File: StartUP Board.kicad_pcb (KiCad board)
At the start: 2 copper layers, 47 x 63.5 mm, 24 parts, among them J1 KEYSW_CONN, U3 ANT13SECQE, U4 D1

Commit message: pcb board progress, schematic should be finalized
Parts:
- removed U4: D1, Package_SON:WSON-6-1EP_2x2mm_P0.65mm_EP1x1.6mm
- added U2: D1, Package_SON:WSON-6-1EP_2x2mm_P0.65mm_EP1x1.6mm, F.Cu at (47.8, 48.5)
- AUX_12V1: value PWR_12V -> 12V_Conn
- C1: value 0.1u -> C1
- C2, C3: value 0.1u -> C3
- C4: value 0.1u -> C4
- GPIO6: value FNR_CONN -> FNR_OUT
- J1: value KEYSW_CONN -> KEYSW_OUT
- R1: value 100k -> R1
- R10: value 30k -> R10
- R2: value 100k -> R2
- R3: value 100k -> R3
- R4: value 100k -> R4
- R5: value 10k -> R5
- R6: value 10k -> R6
- R7: value 10k -> R7
- R8: value 30k -> R8
- R9: value 30k -> R9
- moved R4 1.54 mm to (45.0, 50.0)
- moved C4 1.50 mm to (45.0, 46.8)
- moved REF** 1.41 mm to (38.0, 70.5)
- moved REF** 1.12 mm to (80.0, 70.5)
- moved R3 1.04 mm to (42.5, 50.0)
- moved C3 1.03 mm to (42.5, 46.8)
- moved R5 1.00 mm to (47.5, 54.0)
- moved R8 1.00 mm to (45.0, 54.0)
- moved R2 0.56 mm to (40.0, 50.0)
- moved R6 0.50 mm to (47.5, 57.0)
- moved R9 0.50 mm to (45.0, 57.0)
- moved REF** 0.50 mm to (80.0, 11.5)
- moved REF** 0.50 mm to (38.0, 11.5)
- moved C2 0.48 mm to (40.0, 46.8)
- moved R1 0.25 mm to (37.5, 50.0)
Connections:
- J1 pad 2: Net-(J1-Pin_2) -> Net-(J1-Pin_1)
- J1 pad 3: Net-(J1-Pin_3) -> Net-(J1-Pin_1)
- R10 pad 2: Net-(J1-Pin_3) -> Net-(J1-Pin_1)
- R6 pad 1: Net-(J1-Pin_2) -> Net-(J1-Pin_1)
- R7 pad 1: Net-(J1-Pin_3) -> Net-(J1-Pin_1)
- R9 pad 2: Net-(J1-Pin_2) -> Net-(J1-Pin_1)
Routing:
- net Net-(J1-Pin_1): track 1.50 -> 87.4 mm, vias 0 -> 4
- net /FNR_FWD: track 0.00 -> 38.5 mm, vias 0 -> 2
- net GND: track 0.00 -> 21.3 mm, vias 0 -> 10
- net /KEYSW_CHARGE: track 8.84 -> 26.4 mm
- net +12V: track 4.40 -> 21.5 mm
- net /KEYSW_MAIN: track 11.4 -> 25.0 mm
- net /KEYSW_AUX: track 15.3 -> 26.0 mm
- net /KEYSW_OFF: track 22.2 -> 26.3 mm
- net /FNR_REV: track 36.9 -> 33.6 mm, vias 0 -> 2
- net Net-(J1-Pin_2): track 1.54 -> 0.00 mm
- net Net-(J1-Pin_3): track 1.50 -> 0.00 mm
- added copper zone on B.Cu, net GND
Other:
- board size 47 x 63.5 mm -> 47 x 64 mm
- board text added: "C2"
- board text added: "R1"
- board text added: "empty space below, is bad?"
- board text added: "questions: trace widths correct? used .5mm for 12V and then .3 for everything else holes bad? add CE and DE connectors for e-stop button? via locations weird? this is e stop hole"
- board text added: "to do: add psr stuff"

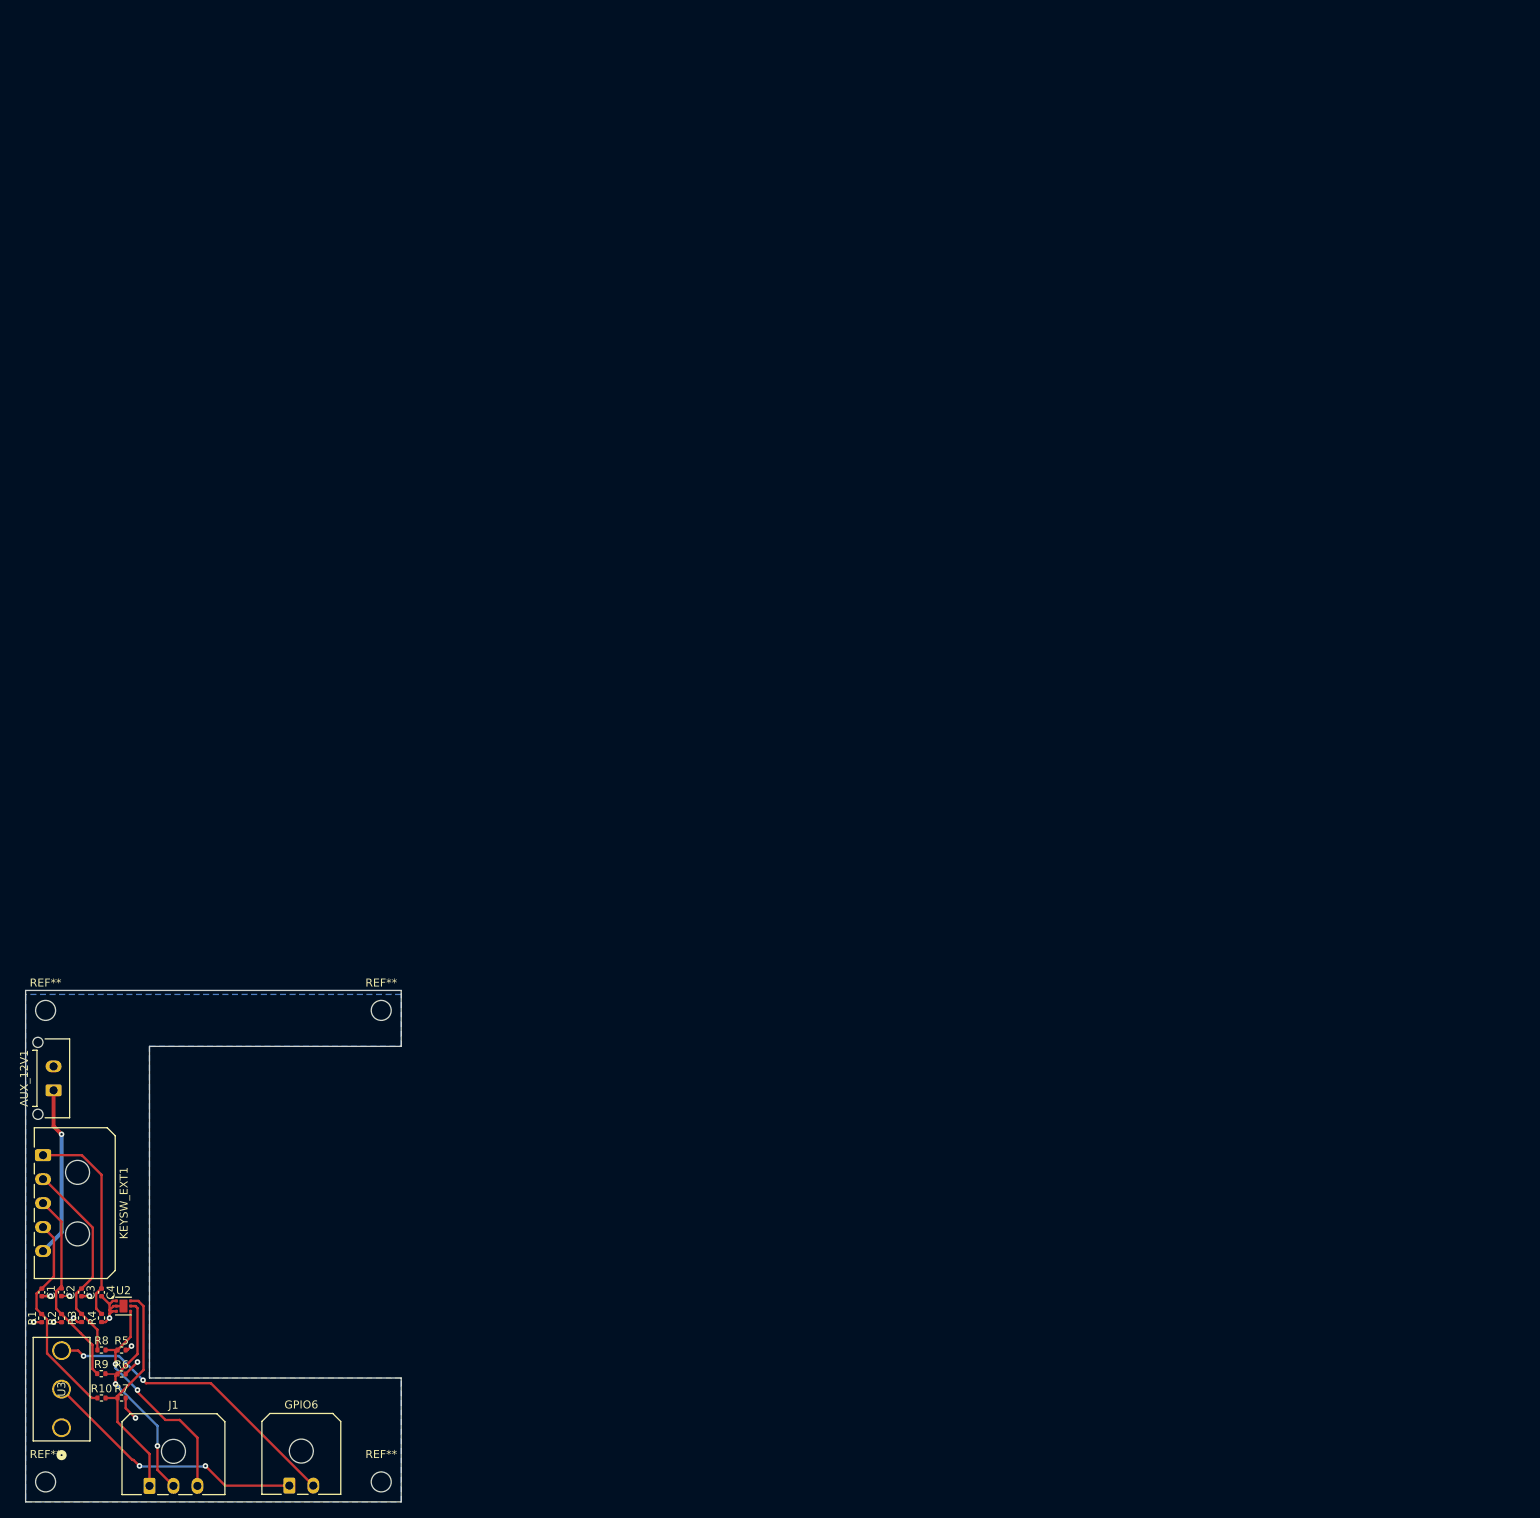
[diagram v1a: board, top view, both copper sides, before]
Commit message: Updated PCB layout, added mounting holes
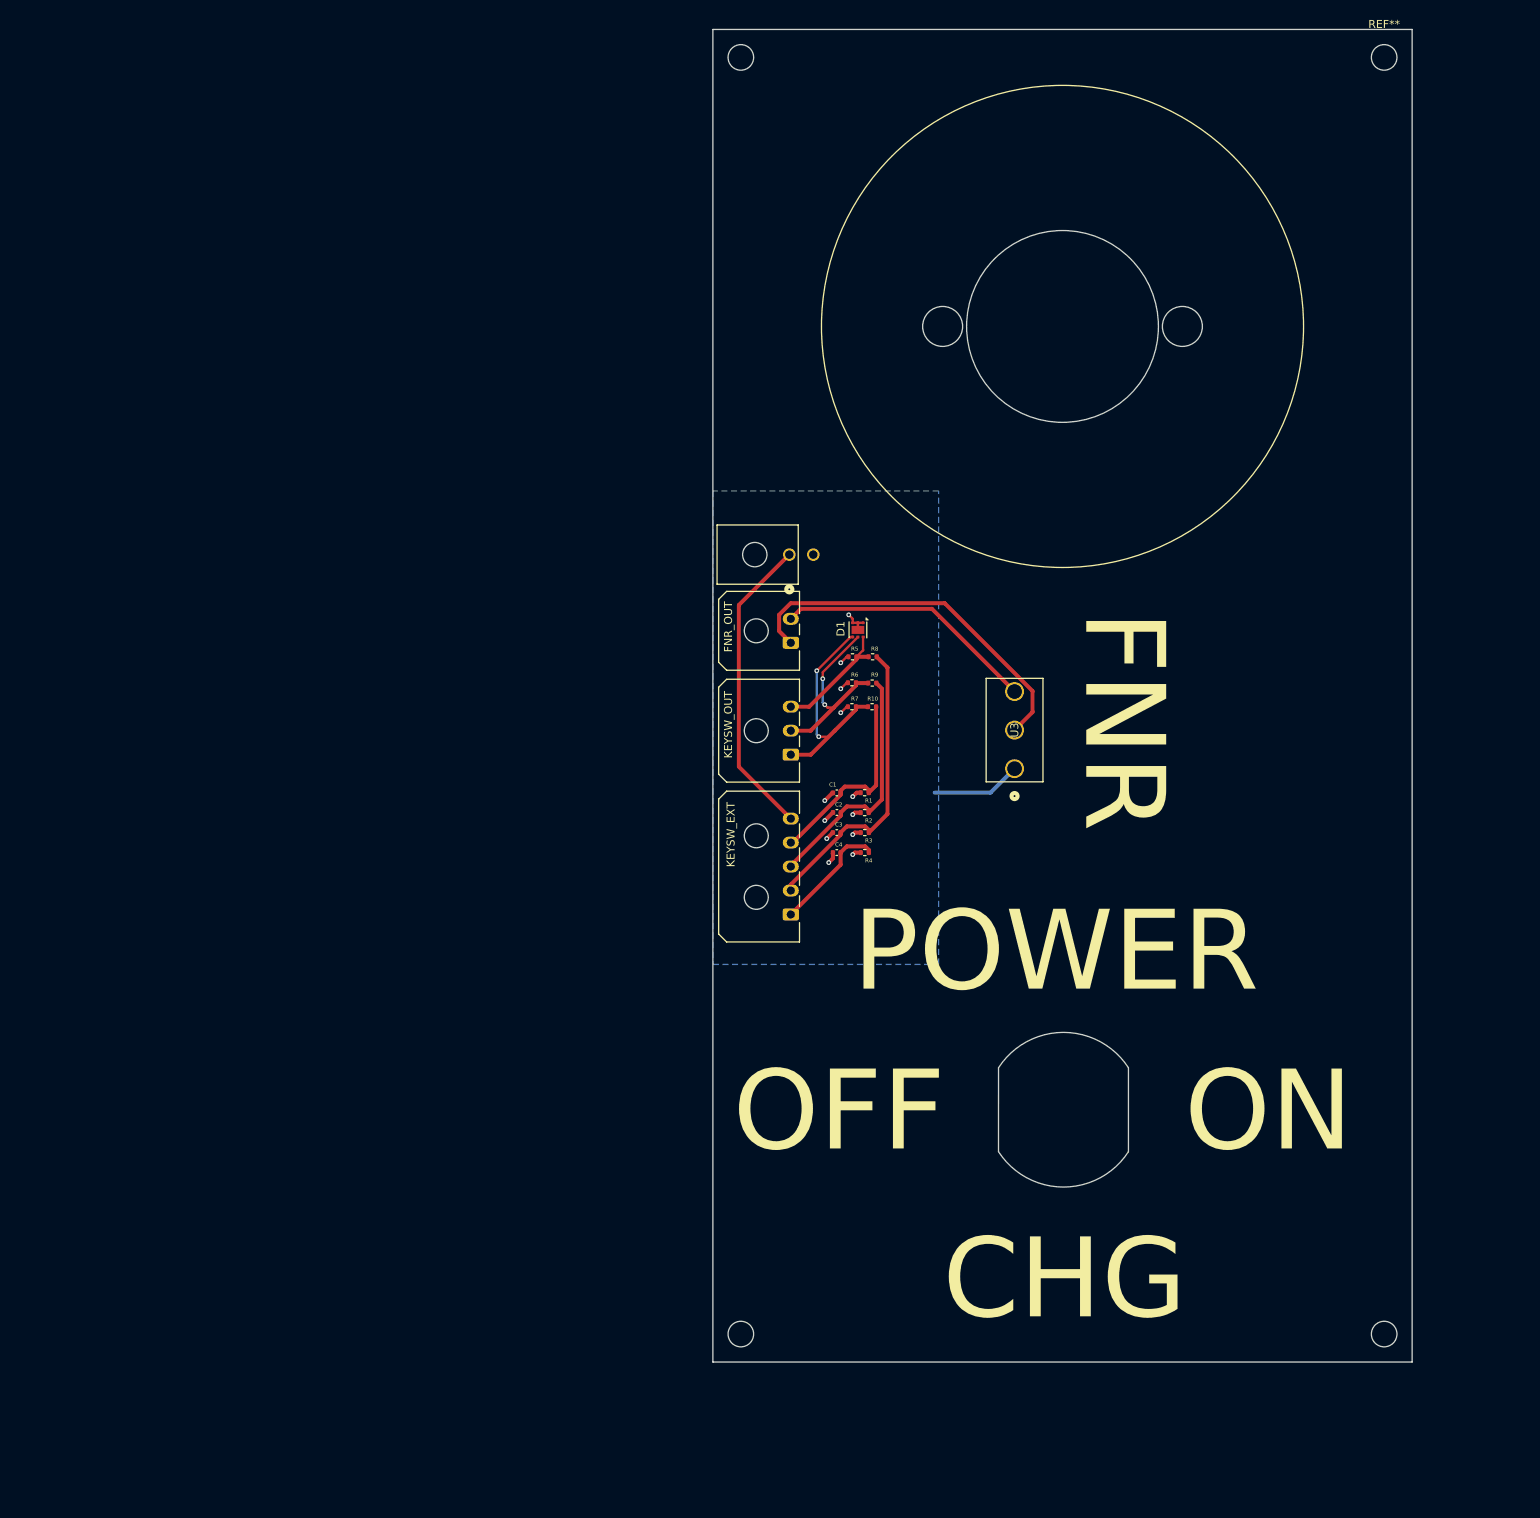
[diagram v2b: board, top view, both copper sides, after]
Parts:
- removed the REF** at (80.0, 70.5)
- removed the REF** at (38.0, 70.5)
- removed the REF** at (80.0, 11.5)
- removed the REF** at (38.0, 11.5)
- added REF**: H2, MountingHole:MountingHole_3.2mm_M3, F.Cu at (125.0, -107.8)
- added REF**: H3, MountingHole:MountingHole_3.2mm_M3, F.Cu at (125.0, 52.0)
- added REF**: H1, MountingHole:MountingHole_3.2mm_M3, F.Cu at (205.5, -107.8)
- added REF**: H4, MountingHole:MountingHole_3.2mm_M3, F.Cu at (205.5, 52.0)
- AUX_12V1: value 12V_Conn -> GND; footprint Connector_Molex:Molex_Micro-Fit_3.0_43650-0215_1x02_P3.00mm_Vertical -> Micro-Fit 3.0 Right-Angle Header:CONN_SD-43045-001_02_MOL
- C2: value C3 -> 0.1u
- R1: value R1 -> 100k
- moved U3 145.0 mm to (159.2, -18.8)
- moved R8 129.8 mm to (141.5, -32.8), turned to 180 degrees
- moved R10 129.5 mm to (141.4, -26.5), turned to 180 degrees
- moved R9 129.5 mm to (141.4, -29.5), turned to 180 degrees
- moved R5 126.1 mm to (139.0, -32.8), turned to 180 degrees
- moved R6 125.8 mm to (138.9, -29.5), turned to 180 degrees
- moved R7 125.8 mm to (138.9, -26.5), turned to 180 degrees
- moved U2 124.9 mm to (139.7, -36.1), turned to -90 degrees
- moved GPIO6 122.7 mm to (131.2, -34.5), turned to 90 degrees
- moved R1 122.2 mm to (140.5, -15.7), turned to 0 degrees
- moved J1 121.7 mm to (131.2, -20.5), turned to 90 degrees
- moved R2 118.7 mm to (140.5, -13.2), turned to 0 degrees
- moved C1 117.5 mm to (137.0, -15.7), turned to 180 degrees
- moved R3 115.3 mm to (140.5, -10.8), turned to 0 degrees
- moved C2 114.1 mm to (137.0, -13.3), turned to 180 degrees
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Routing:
- net Net-(J1-Pin_1): track 87.4 -> 68.6 mm
- net +12V: track 21.5 -> 38.3 mm, vias 1 -> 0
- net /FNR_REV: track 33.6 -> 46.8 mm, vias 2 -> 0
- net /KEYSW_AUX: track 26.0 -> 37.7 mm
- net /KEYSW_OFF: track 26.3 -> 14.7 mm
- net GND: track 21.3 -> 28.2 mm, vias 10 -> 12
- net /KEYSW_MAIN: track 25.0 -> 30.9 mm
- net /FNR_FWD: track 38.5 -> 32.8 mm, vias 2 -> 0
- net /KEYSW_CHARGE: track 26.4 -> 24.6 mm
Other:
- board size 47 x 64 mm -> 87.5 x 166.8 mm
- board text added: "8.7.A.3 switch labels at least 10mm tall - should switch just be seperate? is board too big (too expensive?)"
- board text added: "<-- E-Stop mounting holes"
- board text added: "CHG"
- board text added: "FNR"
- board text added: "OFF"
- board text added: "ON"
- board text added: "POWER"
- board text removed: "FNR_SW"
- board text removed: "empty space below, is bad?"
- board text removed: "questions: trace widths correct? used .5mm for 12V and then .3 for everything else holes bad? add CE and DE connectors for e-stop button? via locations weird? this is e stop hole"
- board text removed: "to do: add psr stuff"

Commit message: moved connectors to the bottom of the pcb, should be mostly finished
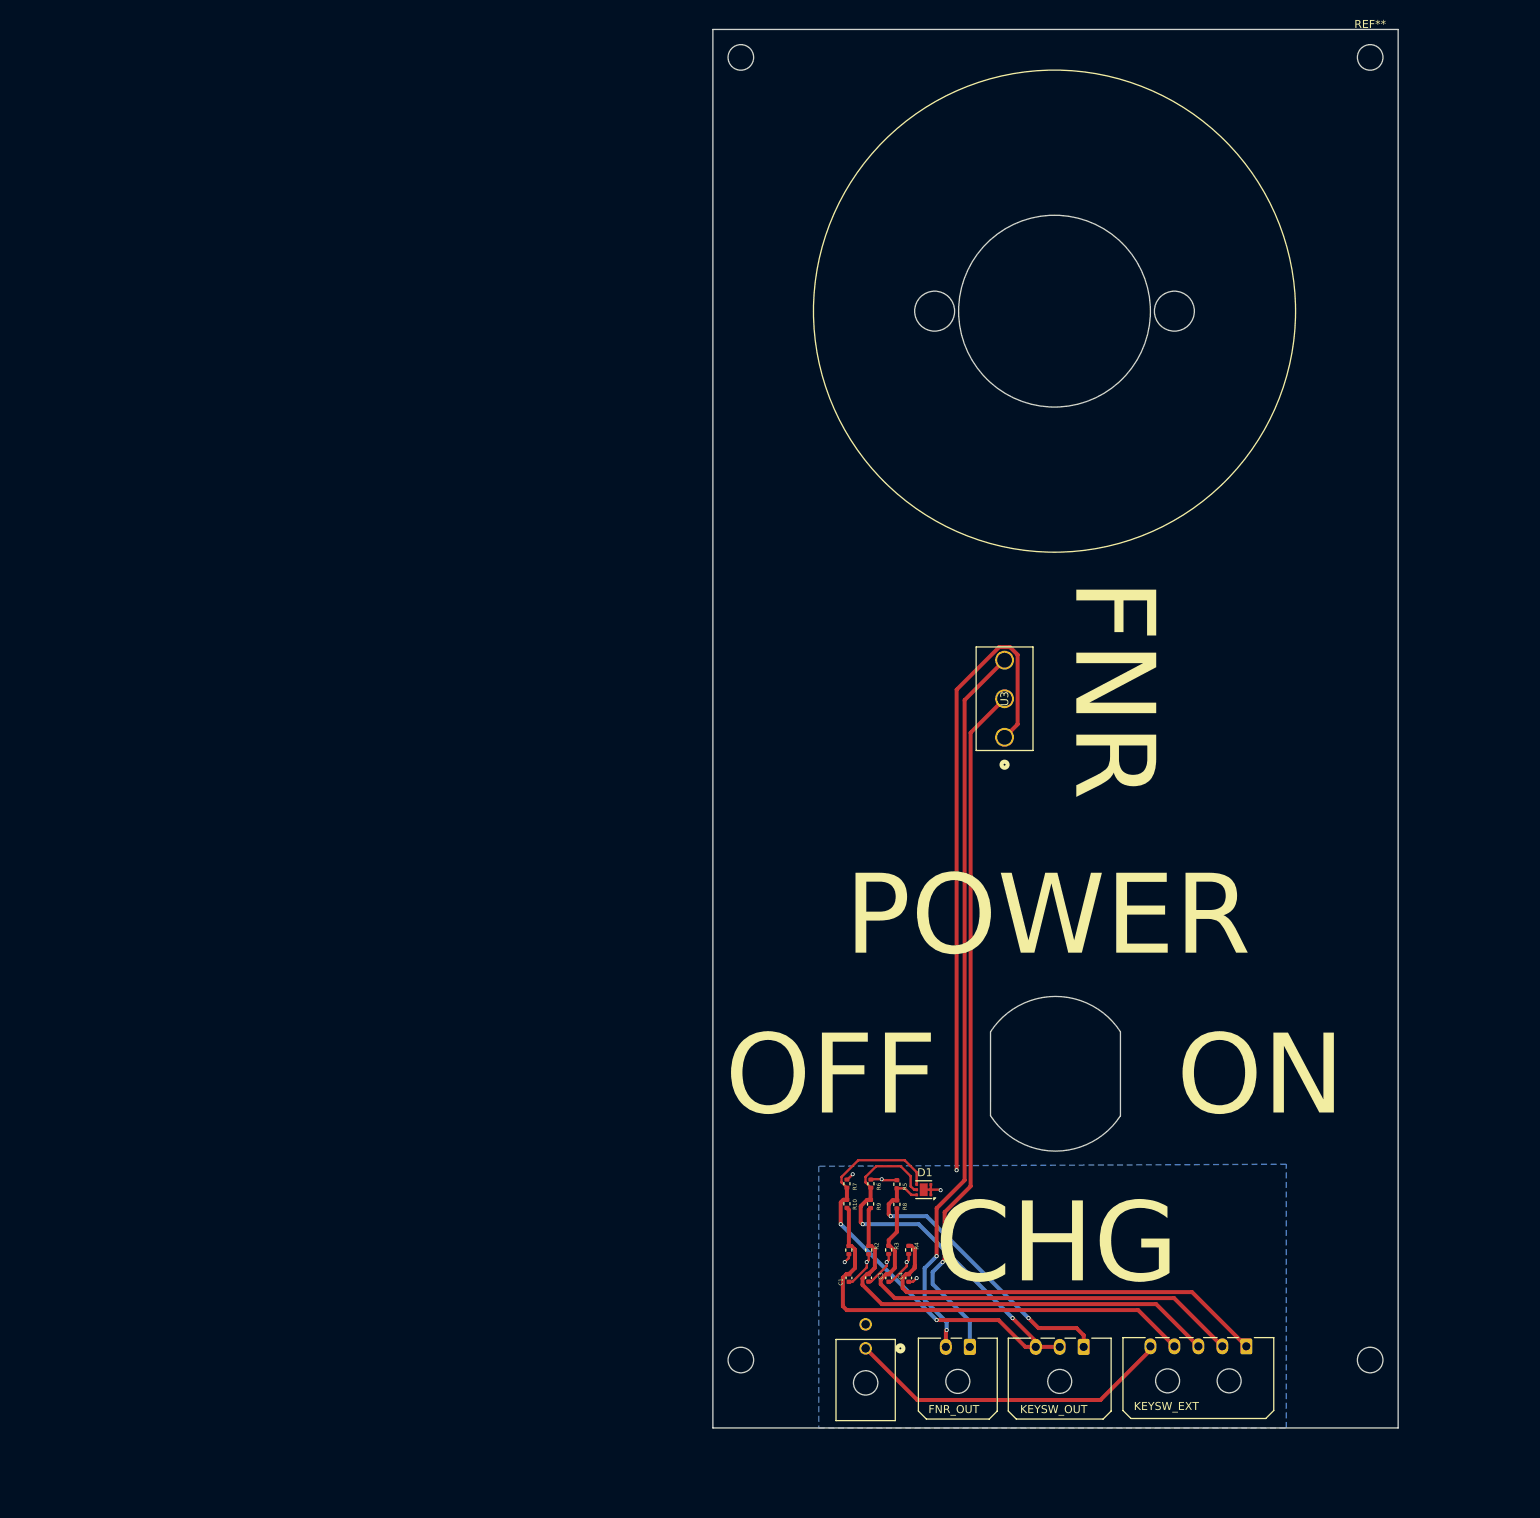
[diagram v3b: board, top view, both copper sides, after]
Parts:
- moved AUX_12V1 99.8 mm to (140.6, 53.8), turned to 0 degrees
- moved GPIO6 90.9 mm to (153.7, 53.6), turned to 180 degrees
- moved J1 82.7 mm to (167.9, 53.6), turned to 180 degrees
- moved KEYSW_EXT1 78.5 mm to (188.2, 53.5), turned to 180 degrees
- moved U2 70.5 mm to (147.9, 33.9), turned to 180 degrees
- moved R8 68.6 mm to (144.5, 35.8), turned to 90 degrees
- moved R5 66.2 mm to (144.5, 33.3), turned to 90 degrees
- moved R9 65.2 mm to (141.2, 35.7), turned to 90 degrees
- moved R6 62.7 mm to (141.3, 33.2), turned to 90 degrees
- moved R10 62.3 mm to (138.3, 35.7), turned to 90 degrees
- moved C1 60.7 mm to (138.5, 45.0), turned to -90 degrees
- moved R7 59.7 mm to (138.3, 33.2), turned to 90 degrees
- moved C2 58.4 mm to (141.0, 45.0), turned to -90 degrees
- moved R1 57.3 mm to (138.5, 41.5), turned to 90 degrees
- moved C3 56.1 mm to (143.5, 45.0), turned to -90 degrees
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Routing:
- net GND: track 28.2 -> 105.7 mm, vias 12 -> 9
- net Net-(J1-Pin_1): track 68.6 -> 135.9 mm, vias 4 -> 6
- net /FNR_FWD: track 32.8 -> 91.3 mm, vias 0 -> 2
- net /FNR_REV: track 46.8 -> 86.8 mm, vias 0 -> 1
- net /KEYSW_OFF: track 14.7 -> 52.6 mm
- net /KEYSW_CHARGE: track 24.6 -> 57.3 mm
- net /KEYSW_MAIN: track 30.9 -> 56.2 mm
- net /KEYSW_AUX: track 37.7 -> 57.2 mm
- net +12V: track 38.3 -> 41.4 mm
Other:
- board size 87.5 x 166.8 mm -> 85.8 x 175 mm
- board text removed: "C2"
- board text removed: "R1"
